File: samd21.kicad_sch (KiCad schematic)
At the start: 32 parts, among them IC1 SAMD21G18A, J1 USB_C, J2 DEBUG, SW5 RESET, U3 GD25Q32C

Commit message: gregdavill: Initial commit of new badge design
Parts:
- removed TP1: PA0, Connectors:TestPoint_Large, symbol Connector:TestPoint
- removed TP14: PA18, Connectors:TestPoint_Large, symbol Connector:TestPoint
- removed TP15: PA17, Connectors:TestPoint_Large, symbol Connector:TestPoint
- added TP17: LE, Connectors:TestPoint_Large, symbol Connector:TestPoint
- added TP18: BLK, Connectors:TestPoint_Large, symbol Connector:TestPoint
- added TP3: DAT, Connectors:TestPoint_Large, symbol Connector:TestPoint
- R9: renamed from R11; value 100k -> 4.7K
- SW5: footprint Button_Switch_SMD:SW_SPST_TL3342 -> Button_Switch_SMD:SW_SPST_PTS810
- TP15: renamed from TP13; value PA19 -> PA0
- TP16: value PA16 -> CLK
- renumbered D25 to D513, R5 to R3, R6 to R4, R7 to R5, R8 to R6, R9 to R7, R10 to R8, TP8 to TP10, TP9 to TP11, TP10 to TP12, TP11 to TP13, TP12 to TP14, TP2 to TP4, TP3 to TP5, TP4 to TP6, TP5 to TP7, TP6 to TP8, TP7 to TP9, U3 to U5
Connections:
- net GND: no longer R9.1
- net SDB: no longer R9.2
- net VCC: now also R9.1
- net at IC1.1 (PA0/XIN32/EIC/SCOM1PAD0/TC2): now also TP15.1
- net LED_BLANK: now reaches IC1.25 (PA16/I2C/EIC/SCOM1PAD0+/TC2)
- net LED_BLANK: now also R9.2, TP18.1; no longer TP16.1
- net LED_LATCH: now reaches IC1.26 (PA17/I2C/EIC/SCOM1PAD1+/TC2)
- net LED_LATCH: now also TP17.1
- net LED_SCLK: now reaches IC1.27 (PA18/EIC/SCOM1PAD2+/TC3)
- net LED_SCLK: now also TP16.1
- net LED_DAT: now reaches IC1.28 (PA19/EIC/SCOM1PAD3+/TC3)
- net LED_DAT: now also TP3.1; no longer TP15.1
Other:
- moved on the sheet: R9, TP15

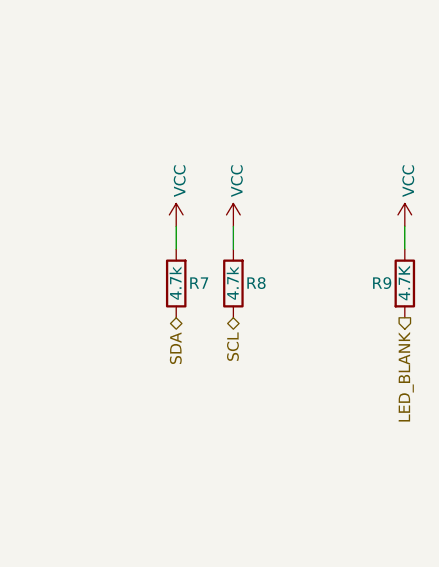
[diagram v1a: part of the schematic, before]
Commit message: add BOM
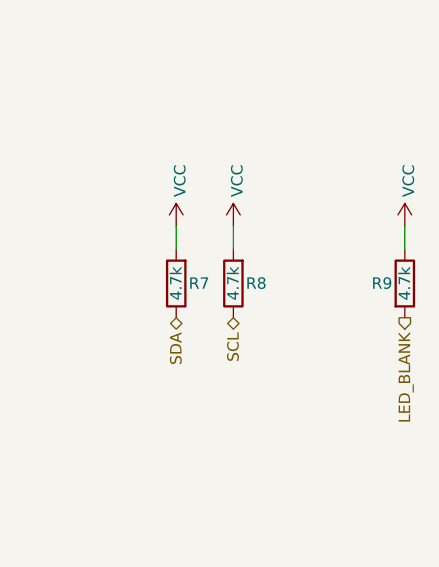
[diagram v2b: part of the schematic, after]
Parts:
- C5: Mfg (none) -> Samsung Electro-Mechanics; PN (none) -> CL10B105KO8NNNC
- C6: Mfg (none) -> Samsung Electro-Mechanics; PN (none) -> CL10B104KB8NNNC
- C7: Mfg (none) -> Samsung Electro-Mechanics; PN (none) -> CL10A106MO8NQNC
- D513: Mfg (none) -> Foshan NationStar Optoelectronics; PN (none) -> NCD0603C1
- IC1: Mfg (none) -> Microchip Tech; PN (none) -> ATSAMD21G16L-MNT
- J1: Mfg (none) -> XKB Connectivity; PN (none) -> U262-161N-4BVC11
- R3, R4: Mfg (none) -> UNI-ROYAL(Uniroyal Elec); PN (none) -> 0603WAF5101T5E
- R5: Mfg (none) -> UNI-ROYAL(Uniroyal Elec); PN (none) -> 0603WAF1002T5E
- R6: Mfg (none) -> UNI-ROYAL(Uniroyal Elec); PN (none) -> 0603WAF1001T5E
- R7, R8: Mfg (none) -> UNI-ROYAL(Uniroyal Elec); PN (none) -> 0603WAF4701T5E
- R9: value 4.7K -> 4.7k; Mfg (none) -> UNI-ROYAL(Uniroyal Elec); PN (none) -> 0603WAF4701T5E
- SW5: Mfg (none) -> C&K; PN (none) -> PTS810SJK250SMTRLFS
- U5: Mfg (none) -> GigaDevice Semicon Beijing; PN (none) -> GD25Q32CSIGR
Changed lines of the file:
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@@
+      (effects (font (size 1.27 1.27)) hide)
+    )
+    (property "Mfg" "UNI-ROYAL(Uniroyal Elec)" (id 4) (at 60.96 40.64 0)
+      (effects (font (size 1.27 1.27)) hide)
+    )
+    (property "PN" "0603WAF5101T5E" (id 5) (at 60.96 40.64 0)
       (effects (font (size 1.27 1.27)) hide)
     )
@@
       (effects (font (size 1.27 1.27)) hide)
     )
+    (property "Mfg" "UNI-ROYAL(Uniroyal Elec)" (id 4) (at 60.96 43.18 0)
+      (effects (font (size 1.27 1.27)) hide)
+    )
+    (property "PN" "0603WAF5101T5E" (id 5) (at 60.96 43.18 0)
+      (effects (font (size 1.27 1.27)) hide)
+    )
   )
   (symbol (lib_id "Device:R") (at 76.2 73.66 180) (unit 1)
@@
       (effects (font (size 1.27 1.27)) hide)
     )
+    (property "Mfg" "UNI-ROYAL(Uniroyal Elec)" (id 4) (at 76.2 73.66 0)
+      (effects (font (size 1.27 1.27)) hide)
+    )
+    (property "PN" "0603WAF1001T5E" (id 5) (at 76.2 73.66 0)
+      (effects (font (size 1.27 1.27)) hide)
+    )
   )
   (symbol (lib_id "Device:R") (at 223.52 58.42 180) (unit 1)
@@
       (effects (font (size 1.27 1.27)) hide)
     )
+    (property "Mfg" "UNI-ROYAL(Uniroyal Elec)" (id 4) (at 223.52 58.42 0)
+      (effects (font (size 1.27 1.27)) hide)
+    )
+    (property "PN" "0603WAF1002T5E" (id 5) (at 223.52 58.42 0)
+      (effects (font (size 1.27 1.27)) hide)
+    )
   )
   (symbol (lib_id "Device:R") (at 234.95 110.49 180) (unit 1)
@@
       (effects (font (size 1.27 1.27)) hide)
     )
+    (property "Mfg" "UNI-ROYAL(Uniroyal Elec)" (id 4) (at 234.95 110.49 0)
+      (effects (font (size 1.27 1.27)) hide)
+    )
+    (property "PN" "0603WAF4701T5E" (id 5) (at 234.95 110.49 0)
+      (effects (font (size 1.27 1.27)) hide)
+    )
   )
   (symbol (lib_id "Device:R") (at 241.3 110.49 180) (unit 1)
@@
       (effects (font (size 1.27 1.27)) hide)
     )
+    (property "Mfg" "UNI-ROYAL(Uniroyal Elec)" (id 4) (at 241.3 110.49 0)
+      (effects (font (size 1.27 1.27)) hide)
+    )
+    (property "PN" "0603WAF4701T5E" (id 5) (at 241.3 110.49 0)
+      (effects (font (size 1.27 1.27)) hide)
+    )
   )
   (symbol (lib_id "Device:R") (at 260.35 110.49 0) (unit 1)
     (in_bom yes) (on_board yes)
     (property "Reference" "R9" (id 0) (at 257.81 110.49 0))
-    (property "Value" "4.7K" (id 1) (at 260.35 110.49 90))
+    (property "Value" "4.7k" (id 1) (at 260.35 110.49 90))
     (property "Footprint" "Resistor_SMD:R_0603_1608Metric" (id 2) (at 258.572 110.49 90)
       (effects (font (size 1.27 1.27)) hide)
     )
     (property "Datasheet" "~" (id 3) (at 260.35 110.49 0)
+      (effects (font (size 1.27 1.27)) hide)
+    )
+    (property "Mfg" "UNI-ROYAL(Uniroyal Elec)" (id 4) (at 260.35 110.49 0)
+      (effects (font (size 1.27 1.27)) hide)
+    )
+    (property "PN" "0603WAF4701T5E" (id 5) (at 260.35 110.49 0)
       (effects (font (size 1.27 1.27)) hide)
     )
@@
     )
     (property "Datasheet" "~" (id 3) (at 76.2 85.09 0)
+      (effects (font (size 1.27 1.27)) hide)
+    )
+    (property "Mfg" "Foshan NationStar Optoelectronics" (id 4) (at 76.2 85.09 0)
+      (effects (font (size 1.27 1.27)) hide)
+    )
+    (property "PN" "NCD0603C1" (id 5) (at 76.2 85.09 0)
       (effects (font (size 1.27 1.27)) hide)
     )
@@
       (effects (font (size 1.27 1.27)) hide)
     )
+    (property "Mfg" "C&K" (id 4) (at 234.95 64.77 0)
+      (effects (font (size 1.27 1.27)) hide)
+    )
+    (property "PN" "PTS810SJK250SMTRLFS" (id 5) (at 234.95 64.77 0)
+      (effects (font (size 1.27 1.27)) hide)
+    )
   )
   (symbol (lib_id "Device:C") (at 29.21 105.41 0) (unit 1)
@@
       (effects (font (size 1.27 1.27)) hide)
     )
+    (property "Mfg" "Samsung Electro-Mechanics" (id 4) (at 29.21 105.41 0)
+      (effects (font (size 1.27 1.27)) hide)
+    )
+    (property "PN" "CL10B104KB8NNNC" (id 5) (at 29.21 105.41 0)
+      (effects (font (size 1.27 1.27)) hide)
+    )
   )
   (symbol (lib_id "Device:C") (at 43.18 105.41 0) (unit 1)
@@
     )
     (property "Datasheet" "~" (id 3) (at 43.18 105.41 0)
+      (effects (font (size 1.27 1.27)) hide)
+    )
+    (property "Mfg" "Samsung Electro-Mechanics" (id 4) (at 43.18 105.41 0)
+      (effects (font (size 1.27 1.27)) hide)
+    )
+    (property "PN" "CL10A106MO8NQNC" (id 5) (at 43.18 105.41 0)
       (effects (font (size 1.27 1.27)) hide)
     )
@@
       (effects (font (size 1.27 1.27)) hide)
     )
+    (property "Mfg" "Samsung Electro-Mechanics" (id 4) (at 203.2 57.15 0)
+      (effects (font (size 1.27 1.27)) hide)
+    )
+    (property "PN" "CL10B105KO8NNNC" (id 5) (at 203.2 57.15 0)
+      (effects (font (size 1.27 1.27)) hide)
+    )
   )
   (symbol (lib_id "Connector:Conn_01x06_Female") (at 118.11 144.78 0) (unit 1)
@@
       (effects (font (size 1.27 1.27)) hide)
     )
+    (property "Mfg" "GigaDevice Semicon Beijing" (id 4) (at 50.8 146.05 0)
+      (effects (font (size 1.27 1.27)) hide)
+    )
+    (property "PN" "GD25Q32CSIGR" (id 5) (at 50.8 146.05 0)
+      (effects (font (size 1.27 1.27)) hide)
+    )
   )
   (symbol (lib_id "Connector:USB_C_Receptacle_USB2.0") (at 38.1 50.8 0) (unit 1)
@@
       (effects (font (size 1.27 1.27)) hide)
     )
+    (property "Mfg" "XKB Connectivity" (id 4) (at 38.1 50.8 0)
+      (effects (font (size 1.27 1.27)) hide)
+    )
+    (property "PN" "U262-161N-4BVC11" (id 5) (at 38.1 50.8 0)
+      (effects (font (size 1.27 1.27)) hide)
+    )
   )
   (symbol (lib_id "samd21g18a:SAMD21G18A") (at 143.51 77.47 0) (unit 1)
@@
       (effects (font (size 1.27 1.27)) hide)
     )
+    (property "Mfg" "Microchip Tech" (id 4) (at 143.51 77.47 0)
+      (effects (font (size 1.27 1.27)) hide)
+    )
+    (property "PN" "ATSAMD21G16L-MNT" (id 5) (at 143.51 77.47 0)
+      (effects (font (size 1.27 1.27)) hide)
+    )
